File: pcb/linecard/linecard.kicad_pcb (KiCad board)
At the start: 6 copper layers, 185 x 93.5 mm, 624 parts, among them J1 CONN_ATX12V, J10 ARF6-08-S-D-A-K-TR, J11 SMPM, J12 SMPM, J13 XILINX_JTAG, J14 ARF6-08-S-D-A-K-TR, J2 LPJT476156AENL, J3 CORTEX_DEBUG_ETM, J4 0532611071, J5 LPJT476156AENL, J6 XILINX_JTAG, J7 SMPM, J8 SMPM, J9 LPJT476156AENL, M1 LONGTHING, M10 SCREWHOLE, M11 SCREWHOLE, M12 960-27-12-D-AB-0, M13 960-27-12-D-AB-0, M2 OSHW, M3 WEEE, M4 SCREWHOLE, M5 SCREWHOLE, M6 SCREWHOLE, M7 SCREWHOLE, M8 SCREWHOLE, M9 SCREWHOLE, SW1 SWITCH, SW2 SWITCH, U1 MYMGK00504ERSR, U10 VSC8512, U11 ESD224DQAR, U12 ESD224DQAR, U13 ESD224DQAR, U14 ESD224DQAR, U15 ESD224DQAR, U16 ESD224DQAR, U17 ESD224DQAR, U18 ESD224DQAR, U19 ESD224DQAR, U2 MYMGK00504ERSR, U20 ESD224DQAR, U21 ESD224DQAR, U22 ESD224DQAR, U23 ESD224DQAR, U24 ESD224DQAR, U25 ESD224DQAR, U26 ESD224DQAR, U27 ESD224DQAR, U28 ESD224DQAR, U29 ESD224DQAR, U3 MYMGK00504ERSR, U30 ESD224DQAR, U31 ESD224DQAR, U32 ESD224DQAR, U33 ESD224DQAR, U34 ESD224DQAR, U35 VSC8512, U36 ESD224DQAR, U37 ESD224DQAR, U38 ESD224DQAR, U39 ESD224DQAR, U4 MYMGK00504ERSR, U40 ESD224DQAR, U41 ESD224DQAR, U42 ESD224DQAR, U43 ESD224DQAR, U44 ESD224DQAR, U45 ESD224DQAR, U46 ESD224DQAR, U47 ESD224DQAR, U48 ESD224DQAR, U49 ESD224DQAR, U5 STM32L431-QFN48, U50 ESD224DQAR, U51 ESD224DQAR, U52 ESD224DQAR, U53 ESD224DQAR, U54 ESD224DQAR, U55 ESD224DQAR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

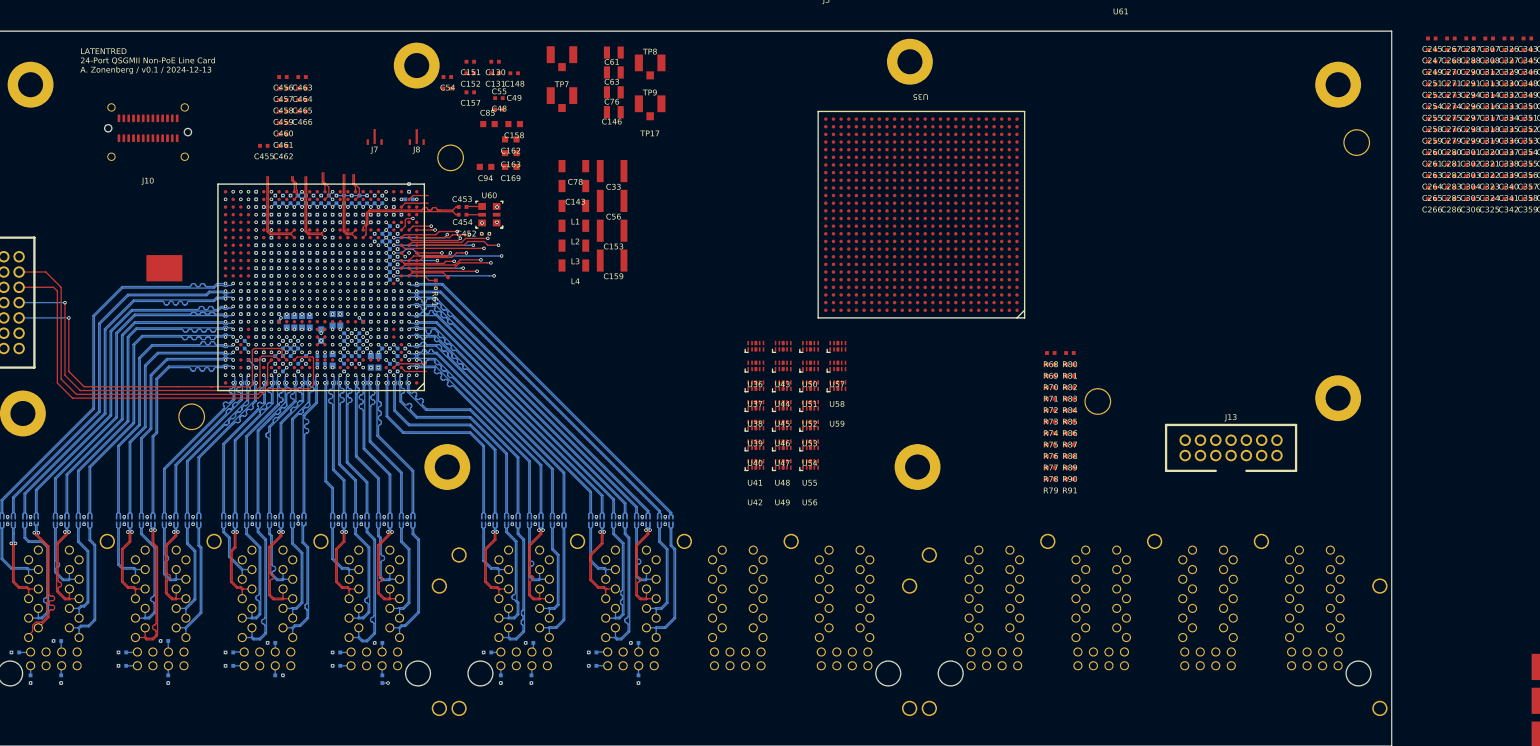
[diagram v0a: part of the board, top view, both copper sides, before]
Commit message: Continued routing left PHY, put right PHY + heatsink in approximately final position
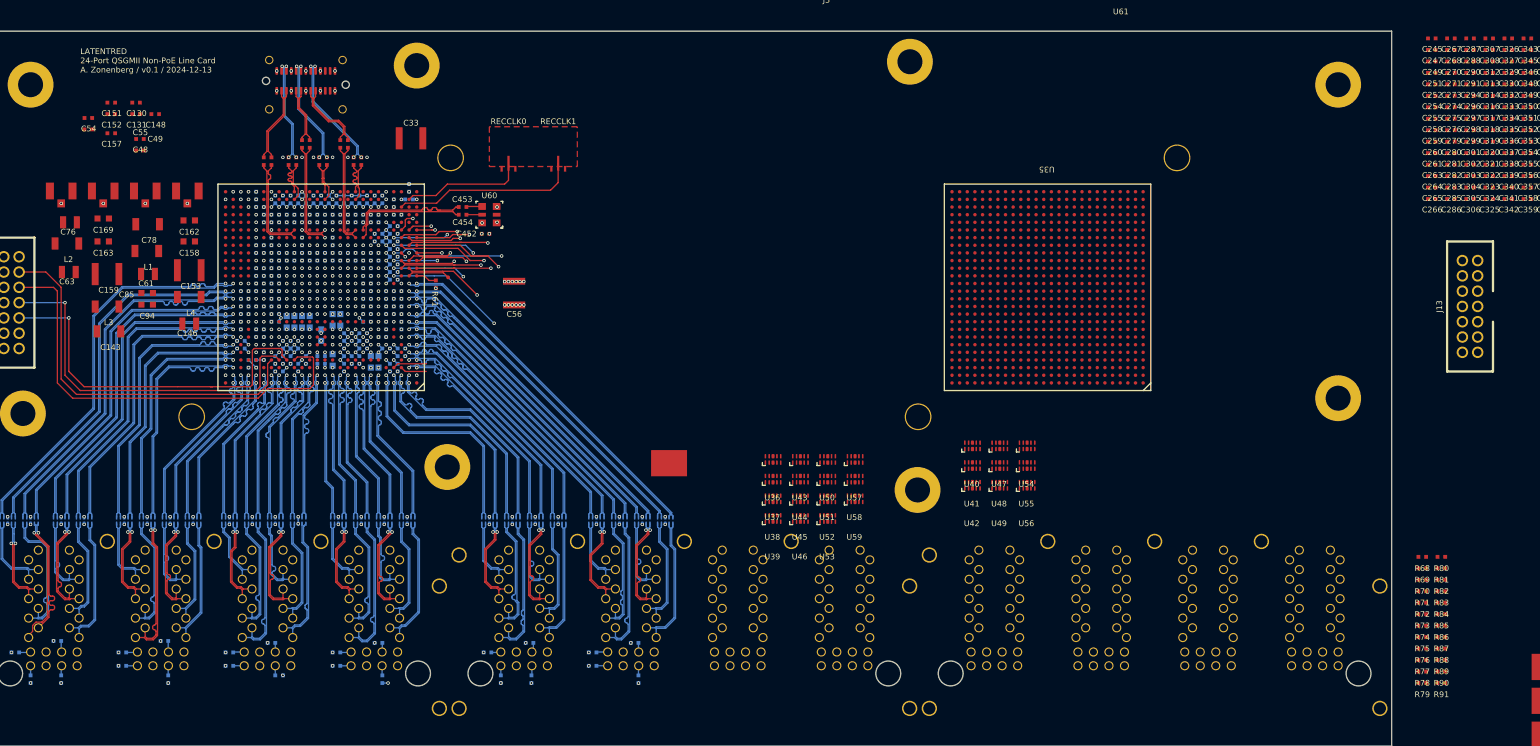
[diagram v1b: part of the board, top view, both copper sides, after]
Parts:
- moved C63 75.9 mm to (41.0, 86.5)
- moved TP9 73.5 mm to (45.5, 76.0)
- moved C76 73.1 mm to (41.1, 80.0)
- moved TP1 70.8 mm to (119.5, 111.5)
- moved C61 67.5 mm to (51.4, 86.8)
- moved TP8 66.7 mm to (40.0, 76.0)
- moved L2 66.3 mm to (40.8, 82.8)
- moved C159 66.1 mm to (46.0, 86.8)
- moved C143 63.7 mm to (46.2, 94.2)
- moved C146 62.0 mm to (56.8, 93.2)
- moved TP17 61.6 mm to (56.5, 76.0)
- moved L3 61.6 mm to (46.0, 91.0)
- moved TP7 57.3 mm to (51.0, 76.0)
- moved C78 56.3 mm to (51.3, 80.2)
- moved L1 56.2 mm to (51.2, 83.7)
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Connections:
- net Net-(J10-RX0_N) renamed /PHY 0 Backend/R0_N
- net Net-(J10-RX0_P) renamed /PHY 0 Backend/R0_P
- net Net-(J10-RX1_N) renamed /PHY 0 Backend/R1_N
- net Net-(J10-RX1_P) renamed /PHY 0 Backend/R1_P
- C457 pad 1: Net-(J10-RX2_P) -> /PHY 0 Backend/R2_N
- C458 pad 1: Net-(J10-RX2_N) -> /PHY 0 Backend/R2_P
- C461 pad 2: Net-(J10-TX0_P) -> /PHY 0 Backend/T0_N
- C462 pad 2: Net-(J10-TX0_N) -> /PHY 0 Backend/T0_P
- C463 pad 2: Net-(J10-TX2_P) -> /PHY 0 Backend/T2_N
- C464 pad 2: Net-(J10-TX2_N) -> /PHY 0 Backend/T2_P
- C465 pad 2: Net-(J10-TX1_P) -> /PHY 0 Backend/T1_N
- C466 pad 2: Net-(J10-TX1_N) -> /PHY 0 Backend/T1_P
- J10 pad 11: Net-(J10-TX1_N) -> /PHY 0 Backend/T1_N
- J10 pad 15: Net-(J10-TX2_P) -> /PHY 0 Backend/T2_P
- J10 pad 16: Net-(J10-RX2_P) -> /PHY 0 Backend/R2_P
- J10 pad 17: Net-(J10-TX2_N) -> /PHY 0 Backend/T2_N
- J10 pad 18: Net-(J10-RX2_N) -> /PHY 0 Backend/R2_N
- J10 pad 3: Net-(J10-TX0_P) -> /PHY 0 Backend/T0_P
- J10 pad 5: Net-(J10-TX0_N) -> /PHY 0 Backend/T0_N
- J10 pad 9: Net-(J10-TX1_P) -> /PHY 0 Backend/T1_P
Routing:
- net /GND: track 958.0 -> 1062.6 mm, vias 284 -> 306
- net /PHY 0 Power/A1V0_VSC: track 50.0 -> 85.4 mm, vias 25 -> 26
- net /PHY 0 Power/A2V5_VSC: track 64.2 -> 91.3 mm, vias 36 -> 37
- net /1V0: track 87.2 -> 108.0 mm, vias 80 -> 86
- net /PHY 0 Backend/CLKOUT1: track 3.71 -> 24.4 mm
- net /PHY 0 Power/A1V0_VSC_SERDES1: track 15.0 -> 31.8 mm, vias 16 -> 17
- net /PHY 0 Backend/T2_N: track 0.00 -> 15.2 mm, vias 0 -> 2
- net /PHY 0 Backend/T2_P: track 0.00 -> 15.2 mm, vias 0 -> 2
- net /PHY 0 Backend/T1_P: track 0.00 -> 14.1 mm, vias 0 -> 2
- net /PHY 0 Backend/T1_N: track 0.00 -> 14.1 mm, vias 0 -> 2
- net /PHY 0 Backend/CLKOUT0: track 2.71 -> 16.3 mm
- net /PHY 0 Backend/T0_P: track 0.00 -> 13.2 mm, vias 0 -> 2
- net /PHY 0 Backend/T0_N: track 0.00 -> 13.2 mm, vias 0 -> 2
- net /PHY 0 Power/A1V0_VSC_SERDES2: track 35.5 -> 46.1 mm, vias 16 -> 17
- net /PHY 0 Backend/R0_P: track 0.00 -> 9.84 mm
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- added copper zone on F.Cu, net /GND
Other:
- board text added: "RECCLK0"
- board text added: "RECCLK1"

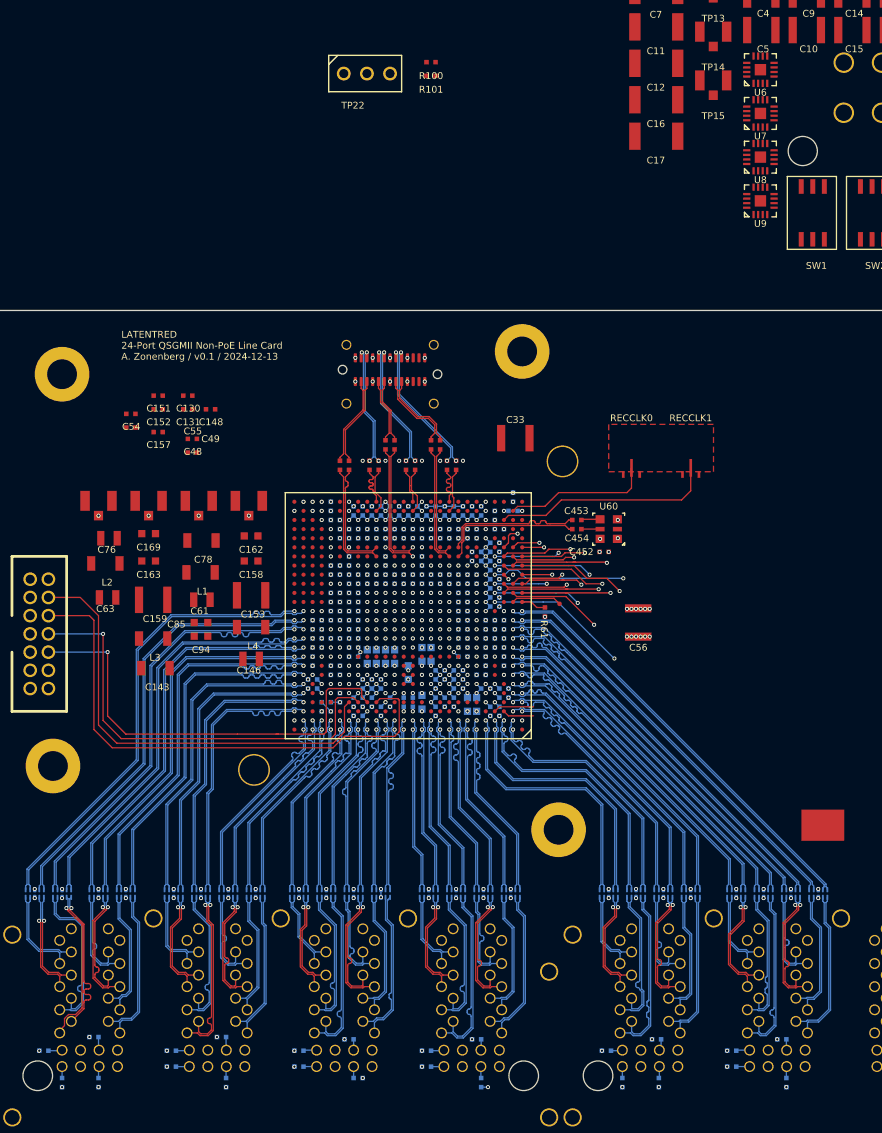
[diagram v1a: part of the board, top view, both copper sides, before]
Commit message: Finished routing of left PHY
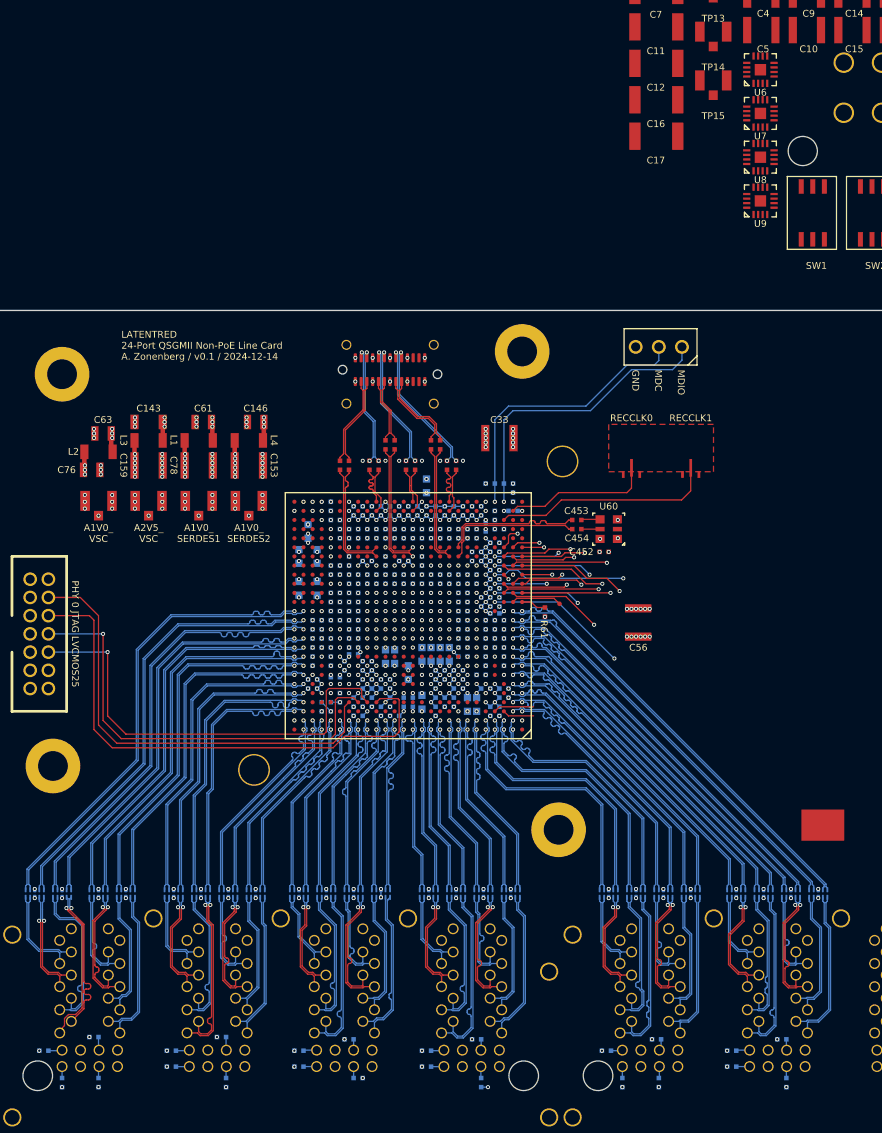
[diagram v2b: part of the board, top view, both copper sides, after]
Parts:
- C130, C131, C148, C151, C152, C157, C158, C162, C163, C169, C48, C49, C54, C55, C85, C94, R100, R101: moved to B.Cu
- C78: footprint azonenberg_pcb:EIA_1206_CAP_NOSILK -> azonenberg_pcb:EIA_1210_CAP_NOSILK
- TP22, TP5, TP6: footprint azonenberg_pcb:CONN_HEADER_2.54MM_1x3 -> azonenberg_pcb:CONN_HEADER_2.54MM_1x3_REFLOW
- moved R100 47.0 mm to (85.0, 74.0)
- moved R101 45.2 mm to (83.0, 74.0), turned to 180 degrees
- moved C55 44.9 mm to (83.5, 88.2)
- moved C54 44.0 mm to (72.5, 99.5)
- moved TP22 43.9 mm to (101.5, 59.0), turned to 180 degrees
- moved C130 38.7 mm to (72.0, 96.0), turned to -90 degrees
- moved C152 36.6 mm to (70.0, 94.0), turned to 90 degrees
- moved C151 36.0 mm to (67.0, 94.0), turned to -90 degrees
- moved C49 35.7 mm to (82.0, 87.0), turned to 90 degrees
- moved C157 34.1 mm to (69.0, 94.0), turned to 90 degrees
- moved C48 33.6 mm to (82.5, 78.8), turned to 90 degrees
- moved C131 31.8 mm to (65.5, 93.5), turned to -90 degrees
- moved C148 28.8 mm to (65.5, 91.5), turned to 90 degrees
- moved C143 27.0 mm to (45.5, 67.2), turned to 180 degrees
- moved C146 26.0 mm to (57.2, 67.2), turned to 180 degrees
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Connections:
- C244 pad 1: /1V0 -> /1V0_2
- C262 pad 1: /1V0 -> /1V0_2
- C61 pad 1: /1V0 -> /1V0_2
- C63 pad 1: /1V0 -> /1V0_2
- L1 pad 2: /1V0 -> /1V0_2
- L2 pad 2: /1V0 -> /1V0_2
- L5 pad 2: /1V0 -> /1V0_2
- L8 pad 2: /1V0 -> /1V0_2
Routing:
- net /GND: track 1062.6 -> 1191.0 mm, vias 306 -> 382
- net /2V5: track 59.7 -> 141.9 mm, vias 21 -> 44
- net /1V0_2: track 0.00 -> 67.4 mm, vias 0 -> 9
- net /3V3: track 321.0 -> 366.2 mm
- net /MDIO: track 0.00 -> 32.7 mm, vias 0 -> 1
- net /MDC: track 0.00 -> 31.2 mm, vias 0 -> 1
- net /PHY 0 Power/A2V5_VSC: track 91.3 -> 110.3 mm, vias 37 -> 47
- net /PHY 0 Power/A1V0_VSC_SERDES1: track 31.8 -> 46.7 mm, vias 17 -> 25
- net /PHY 0 Power/A1V0_VSC_SERDES2: track 46.1 -> 60.4 mm, vias 17 -> 38
- net /PHY 0 Power/A1V0_VSC: track 85.4 -> 98.2 mm, vias 26 -> 37
- net /1V0: track 108.0 -> 118.7 mm, vias 86 -> 88
- net Net-(U10B-PHY10_LED1): track 70.3 -> 68.2 mm
- net /PHY 0 MDI/PHY2_D1_P: track 29.6 -> 31.1 mm
- net /PHY 0 MDI/PHY8_D3_P: track 28.0 -> 29.2 mm
- net /PHY 0 MDI/PHY8_D2_P: track 27.8 -> 28.9 mm
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- added copper zone on In2.Cu, net /1V0
- added copper zone on In2.Cu, net /PHY 0 Power/A1V0_VSC_SERDES1
- added copper zone on In3.Cu, net /PHY 0 Power/A1V0_VSC_SERDES2
- added copper zone on In2.Cu, net /PHY 0 Power/A2V5_VSC
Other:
- board text added: "A1V0_ SERDES1"
- board text added: "A1V0_ SERDES2"
- board text added: "A1V0_ VSC"
- board text added: "A2V5_ VSC"
- board text added: "GND"
- board text added: "LATENTRED 24-Port QSGMII Non-PoE Line Card A. Zonenberg / v0.1 / 2024-12-14"
- board text added: "MDC"
- board text added: "MDIO"
- board text added: "PHY 0 JTAG LVCMOS25"
- board text removed: "LATENTRED 24-Port QSGMII Non-PoE Line Card A. Zonenberg / v0.1 / 2024-12-13"

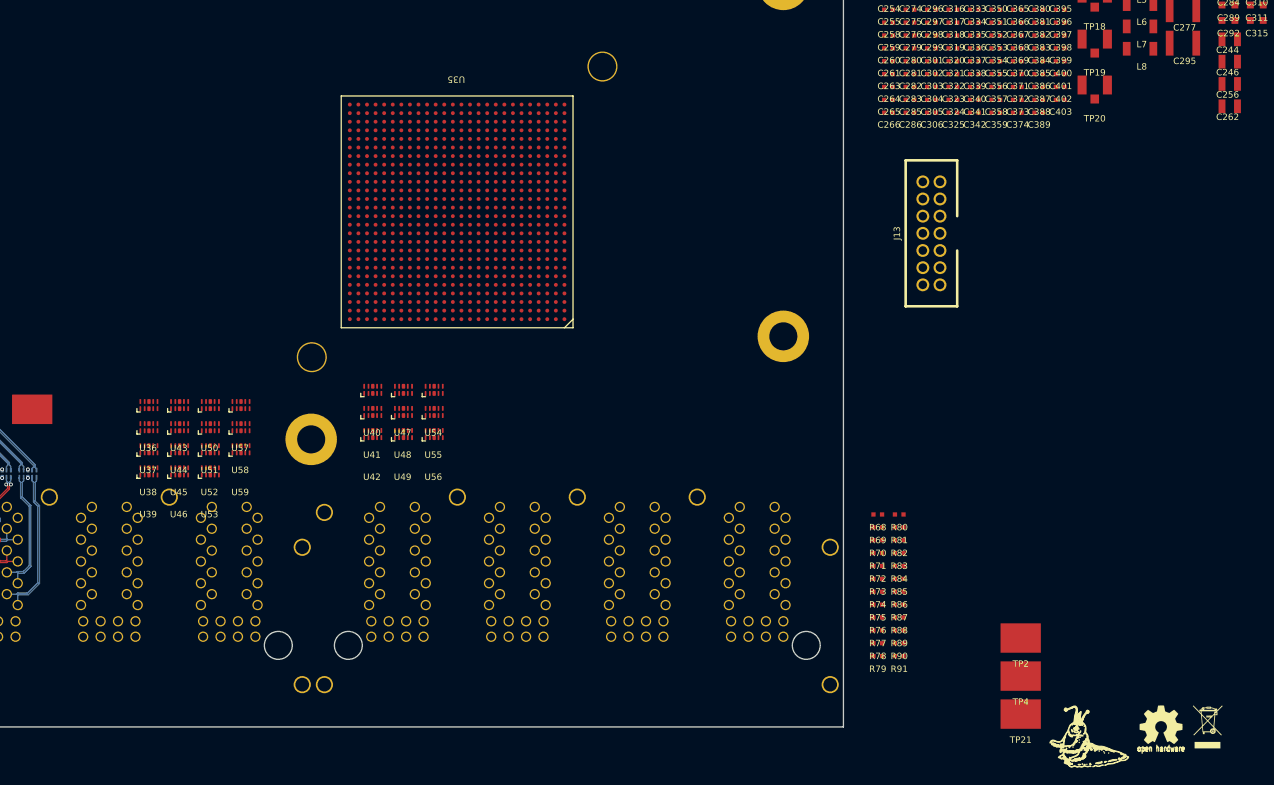
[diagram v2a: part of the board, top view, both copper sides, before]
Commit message: Preliminary placement of ESD diodes for right PHY
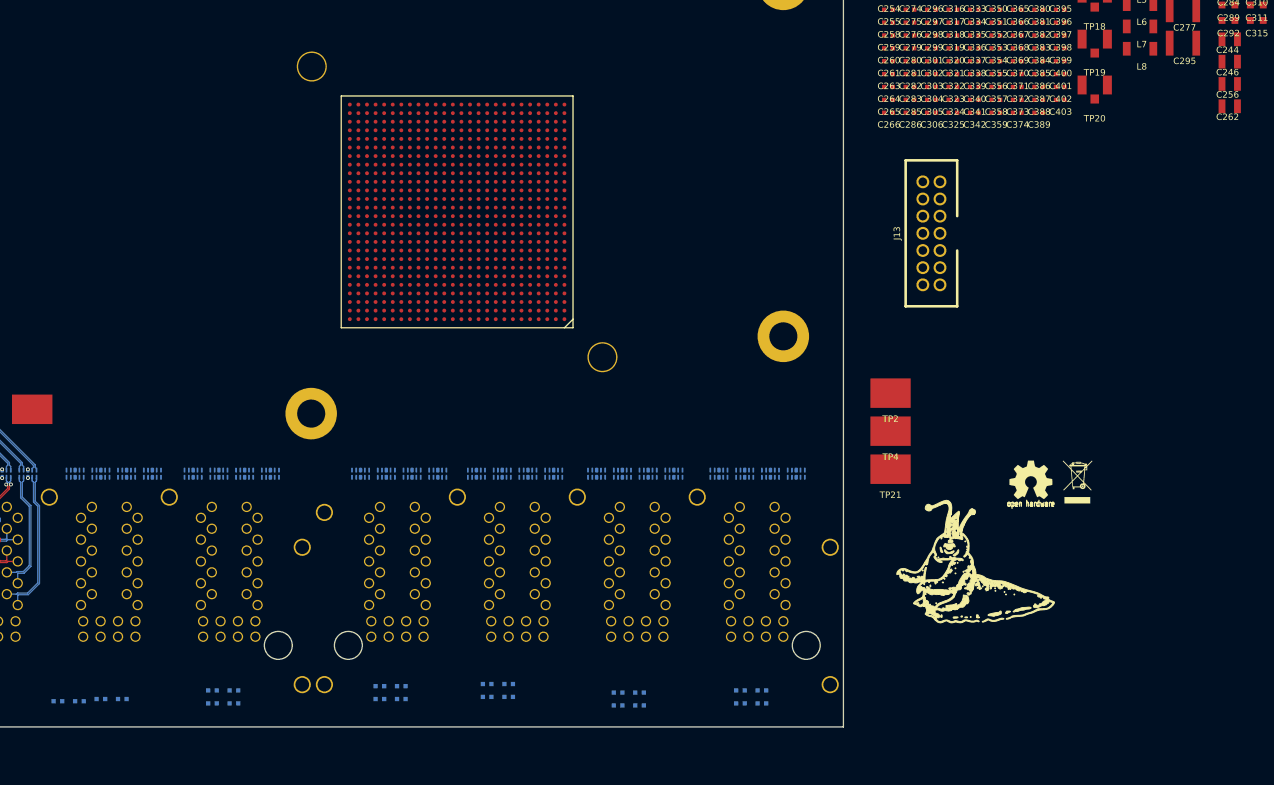
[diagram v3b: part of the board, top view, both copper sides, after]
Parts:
- M1: footprint azonenberg_pcb:LONGTHING-1200DPI -> azonenberg_pcb:LONGTHING-600DPI
- R68, R69, R70, R71, R72, R73, R74, R75, R76, R77, R78, R79, R80, R81, R82, R83, R84, R85, R86, R87, R88, R89, R90, R91, U36, U37, U38, U39, U40, U41, U42, U43, U44, U45, U46, U47, U48, U49, U50, U51, U52, U53, U54, U55, U56, U57, U58, U59: moved to B.Cu
- moved R80 100.4 mm to (122.5, 145.5), turned to 180 degrees
- moved R68 95.5 mm to (125.0, 145.5), turned to 180 degrees
- moved R81 95.1 mm to (127.5, 145.2), turned to 180 degrees
- moved R69 90.2 mm to (130.0, 145.2), turned to 180 degrees
- moved R82 81.9 mm to (140.5, 144.2), turned to 180 degrees
- moved R83 81.9 mm to (140.5, 145.8), turned to 180 degrees
- moved R70 77.0 mm to (143.0, 144.2), turned to 180 degrees
- moved R71 77.0 mm to (143.0, 145.8), turned to 180 degrees
- moved U58 64.9 mm to (208.5, 119.0), turned to 180 degrees
- moved R84 62.1 mm to (160.0, 143.8), turned to 180 degrees
- moved R85 62.1 mm to (160.0, 145.2), turned to 180 degrees
- moved U59 61.7 mm to (205.5, 119.0), turned to 180 degrees
- moved R72 57.2 mm to (162.5, 143.8), turned to 180 degrees
- moved R73 57.2 mm to (162.5, 145.2), turned to 180 degrees
- moved U57 56.2 mm to (199.5, 119.0), turned to 180 degrees
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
